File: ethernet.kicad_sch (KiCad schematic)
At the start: 23 parts, among them J200 RJ45_Hanrun_HR911105A_Horizon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, U200 LAN8742A, Y200 25MHz

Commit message: fix: Silkscreen overlaps
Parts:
- C201, C202, C203, C204, C205, C206, C207, C208: footprint Capacitor_SMD:C_0402_1005Metric -> Library:C_0402_1005Metric
- R200, R201, R202, R203, R204, R205, R206, R207, R208, R209, R210: footprint Resistor_SMD:R_0402_1005Metric -> Library:R_0402_1005Metric
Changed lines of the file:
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@@
 			)
 		)
-		(property "Footprint" "Capacitor_SMD:C_0402_1005Metric"
+		(property "Footprint" "Library:C_0402_1005Metric"
 			(at 42.8752 149.86 0)
 			(effects
@@
 			)
 		)
-		(property "Footprint" "Capacitor_SMD:C_0402_1005Metric"
+		(property "Footprint" "Library:C_0402_1005Metric"
 			(at 103.8352 63.5 0)
 			(effects
@@
 			)
 		)
-		(property "Footprint" "Resistor_SMD:R_0402_1005Metric"
+		(property "Footprint" "Library:R_0402_1005Metric"
 			(at 133.096 78.994 90)
 			(effects
@@
 			)
 		)
-		(property "Footprint" "Resistor_SMD:R_0402_1005Metric"
+		(property "Footprint" "Library:R_0402_1005Metric"
 			(at 58.674 109.474 90)
 			(effects
@@
 			)
 		)
-		(property "Footprint" "Capacitor_SMD:C_0402_1005Metric"
+		(property "Footprint" "Library:C_0402_1005Metric"
 			(at 50.4952 57.15 0)
 			(effects
@@
 			)
 		)
-		(property "Footprint" "Capacitor_SMD:C_0402_1005Metric"
+		(property "Footprint" "Library:C_0402_1005Metric"
 			(at 73.3552 57.15 0)
 			(effects
@@
 			)
 		)
-		(property "Footprint" "Resistor_SMD:R_0402_1005Metric"
+		(property "Footprint" "Library:R_0402_1005Metric"
 			(at 62.484 94.234 90)
 			(effects
@@
 			)
 		)
-		(property "Footprint" "Resistor_SMD:R_0402_1005Metric"
+		(property "Footprint" "Library:R_0402_1005Metric"
 			(at 167.386 78.994 90)
 			(effects
@@
 			)
 		)
-		(property "Footprint" "Capacitor_SMD:C_0402_1005Metric"
+		(property "Footprint" "Library:C_0402_1005Metric"
 			(at 185.1152 152.4 0)
 			(effects
@@
 			)
 		)
-		(property "Footprint" "Capacitor_SMD:C_0402_1005Metric"
+		(property "Footprint" "Library:C_0402_1005Metric"
 			(at 115.2652 63.5 0)
 			(effects
@@
 			)
 		)
-		(property "Footprint" "Resistor_SMD:R_0402_1005Metric"
+		(property "Footprint" "Library:R_0402_1005Metric"
 			(at 134.366 106.934 90)
 			(effects
@@
 			)
 		)
-		(property "Footprint" "Capacitor_SMD:C_0402_1005Metric"
+		(property "Footprint" "Library:C_0402_1005Metric"
 			(at 58.1152 149.86 0)
 			(effects
@@
 			)
 		)
-		(property "Footprint" "Resistor_SMD:R_0402_1005Metric"
+		(property "Footprint" "Library:R_0402_1005Metric"
 			(at 144.526 78.994 90)
 			(effects
@@
 			)
 		)
-		(property "Footprint" "Capacitor_SMD:C_0402_1005Metric"
+		(property "Footprint" "Library:C_0402_1005Metric"
 			(at 61.9252 57.15 0)
 			(effects
@@
 			)
 		)
-		(property "Footprint" "Resistor_SMD:R_0402_1005Metric"
+		(property "Footprint" "Library:R_0402_1005Metric"
 			(at 257.556 138.684 90)
 			(effects
@@
 			)
 		)
-		(property "Footprint" "Resistor_SMD:R_0402_1005Metric"
+		(property "Footprint" "Library:R_0402_1005Metric"
 			(at 114.046 114.554 90)
 			(effects
@@
 			)
 		)
-		(property "Footprint" "Resistor_SMD:R_0402_1005Metric"
+		(property "Footprint" "Library:R_0402_1005Metric"
 			(at 49.276 76.454 90)
 			(effects
@@
 			)
 		)
-		(property "Footprint" "Resistor_SMD:R_0402_1005Metric"
+		(property "Footprint" "Library:R_0402_1005Metric"
 			(at 248.666 148.844 90)
 			(effects
@@
 			)
 		)
-		(property "Footprint" "Resistor_SMD:R_0402_1005Metric"
+		(property "Footprint" "Library:R_0402_1005Metric"
 			(at 155.956 78.994 90)
 			(effects

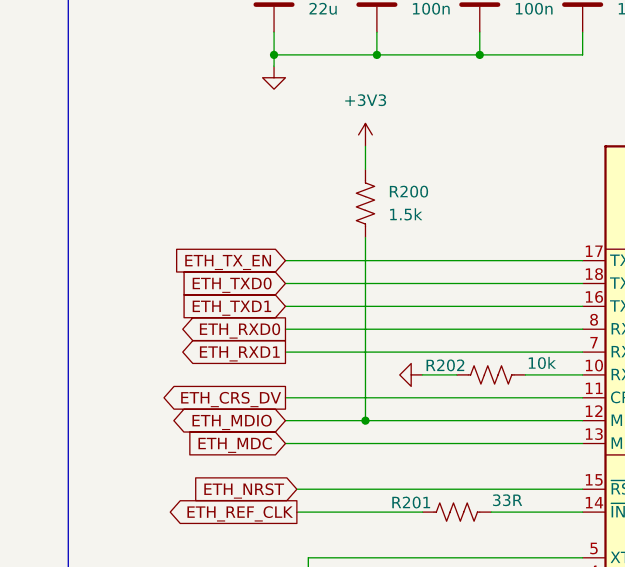
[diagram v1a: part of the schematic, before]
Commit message: Rev 1B - Fix silkscreen, board outline, ethernet pinout
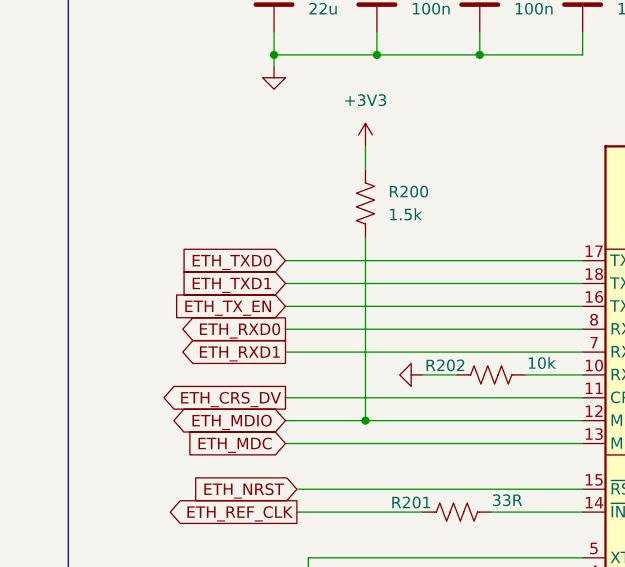
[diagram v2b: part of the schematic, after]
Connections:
- net ETH_TXD0: now also U200.17 (TXD0); no longer U200.18 (TXD1)
- net ETH_TXD1: now also U200.18 (TXD1); no longer U200.16 (TXEN)
- net ETH_TX_EN: now also U200.16 (TXEN); no longer U200.17 (TXD0)
